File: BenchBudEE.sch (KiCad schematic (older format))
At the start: 0 parts

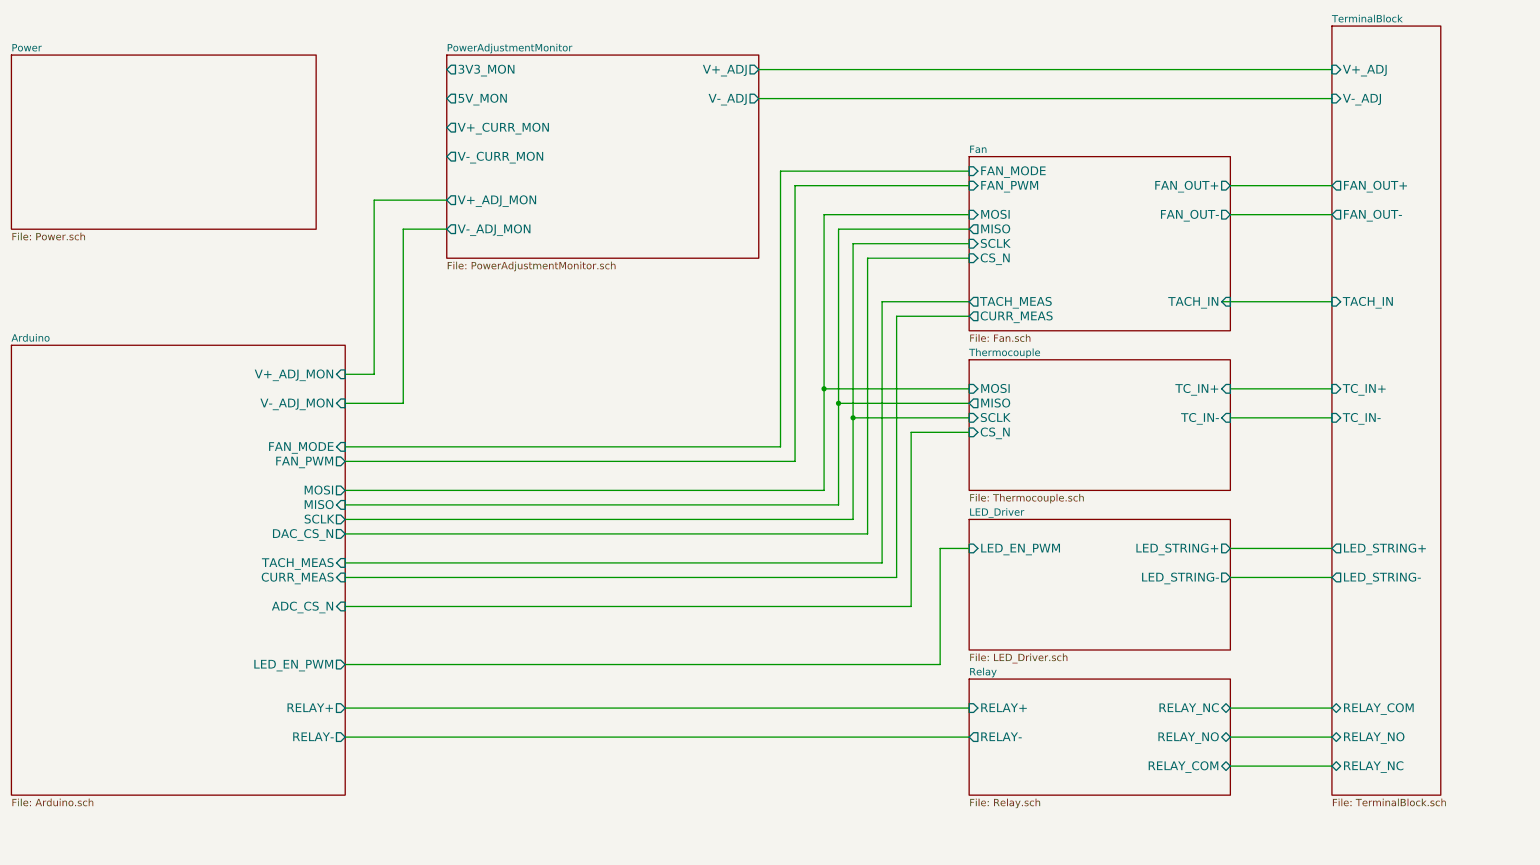
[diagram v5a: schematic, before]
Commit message: Associated and placed the thermocouple module
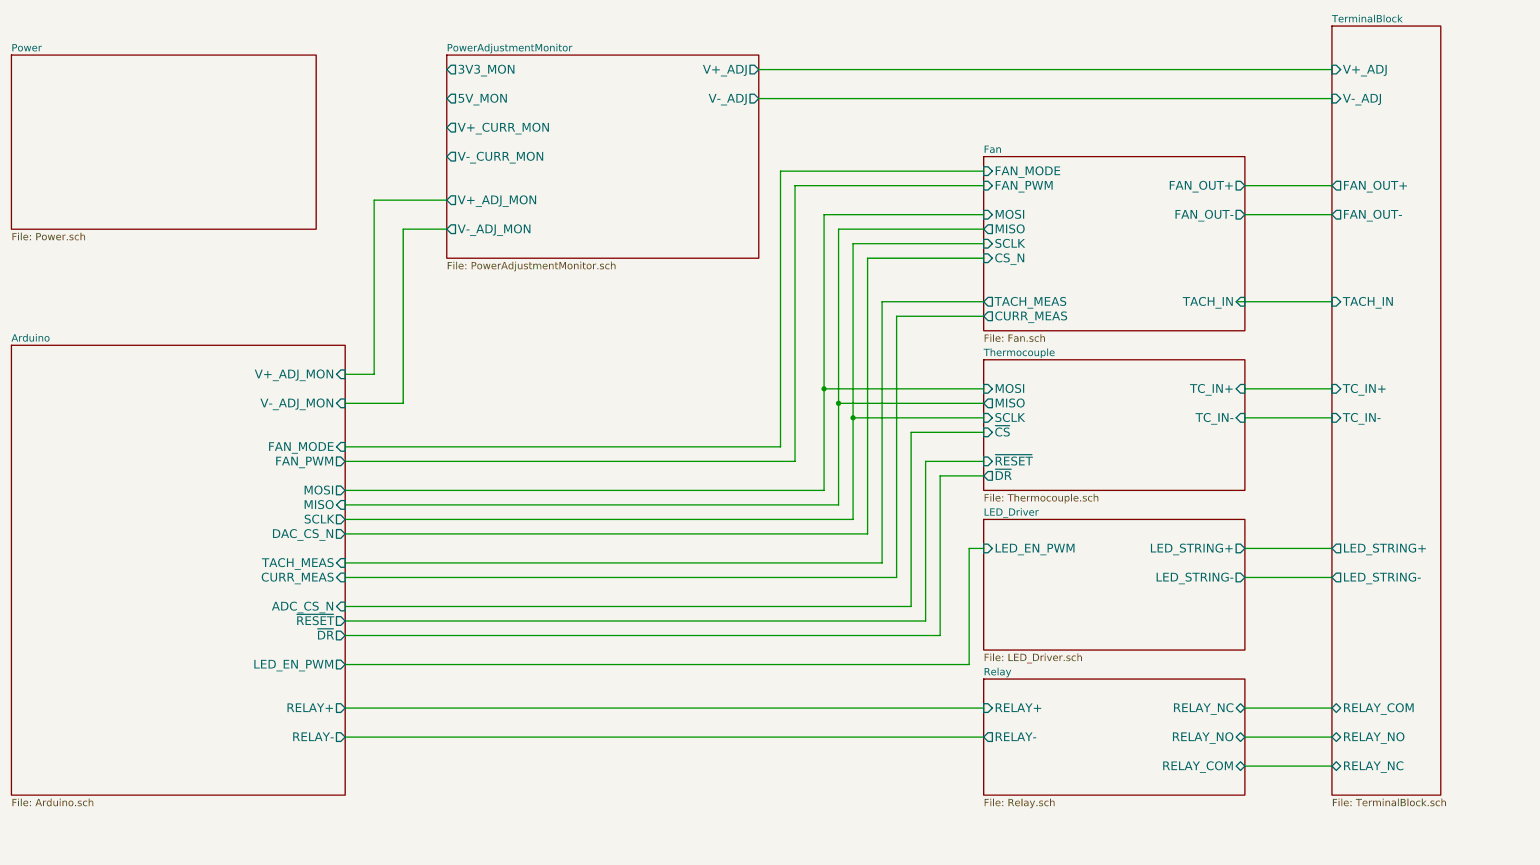
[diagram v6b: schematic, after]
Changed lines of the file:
@@
 $EndDescr
 $Sheet
-S 7500 5300 1800 800
+S 7600 5300 1800 800
 U 52EAE4BD
 F0 "Relay" 50
 F1 "Relay.sch" 50
-F2 "RELAY_NC" B R 9300 5500 60
-F3 "RELAY_NO" B R 9300 5700 60
-F4 "RELAY_COM" B R 9300 5900 60
-F5 "RELAY+" I L 7500 5500 60
-F6 "RELAY-" O L 7500 5700 60
-$EndSheet
-$Sheet
-S 7500 4200 1800 900
+F2 "RELAY_NC" B R 9400 5500 60
+F3 "RELAY_NO" B R 9400 5700 60
+F4 "RELAY_COM" B R 9400 5900 60
+F5 "RELAY+" I L 7600 5500 60
+F6 "RELAY-" O L 7600 5700 60
+$EndSheet
+$Sheet
+S 7600 4200 1800 900
 U 52EAE512
 F0 "LED_Driver" 50
 F1 "LED_Driver.sch" 50
-F2 "LED_EN_PWM" I L 7500 4400 60
-F3 "LED_STRING+" O R 9300 4400 60
-F4 "LED_STRING-" O R 9300 4600 60
+F2 "LED_EN_PWM" I L 7600 4400 60
+F3 "LED_STRING+" O R 9400 4400 60
+F4 "LED_STRING-" O R 9400 4600 60
 $EndSheet
 $Sheet
@@
 	10000 1300 6050 1300
 Wire Wire Line
-	10000 1900 9300 1900
-Wire Wire Line
-	10000 2100 9300 2100
-Wire Wire Line
-	9250 2700 10000 2700
-Wire Wire Line
-	10000 3300 9300 3300
-Wire Wire Line
-	10000 3500 9300 3500
-Wire Wire Line
-	10000 4400 9300 4400
-Wire Wire Line
-	10000 4600 9300 4600
-Wire Wire Line
-	10000 5500 9300 5500
-Wire Wire Line
-	10000 5700 9300 5700
-Wire Wire Line
-	10000 5900 9300 5900
+	10000 1900 9400 1900
+Wire Wire Line
+	10000 2100 9400 2100
+Wire Wire Line
+	9350 2700 10000 2700
+Wire Wire Line
+	10000 3300 9400 3300
+Wire Wire Line
+	10000 3500 9400 3500
+Wire Wire Line
+	10000 4400 9400 4400
+Wire Wire Line
+	10000 4600 9400 4600
+Wire Wire Line
+	10000 5500 9400 5500
+Wire Wire Line
+	10000 5700 9400 5700
+Wire Wire Line
+	10000 5900 9400 5900
 Wire Wire Line
 	3200 3200 3400 3200
@@
 	6300 3800 6300 1900
 Wire Wire Line
-	6300 1900 7500 1900
+	6300 1900 7600 1900
 Wire Wire Line
 	6500 4000 3200 4000
@@
 	6500 2100 6500 4000
 Wire Wire Line
-	6500 2100 7500 2100
+	6500 2100 7600 2100
 Wire Wire Line
 	6600 4100 3200 4100
@@
 	6600 2200 6600 4100
 Wire Wire Line
-	6600 2200 7500 2200
+	6600 2200 7600 2200
 Wire Wire Line
 	6700 4200 3200 4200
@@
 	6700 2300 6700 4200
 Wire Wire Line
-	6700 2300 7500 2300
+	6700 2300 7600 2300
 Wire Wire Line
 	3200 4300 6800 4300
@@
 	6800 4300 6800 2400
 Wire Wire Line
-	6800 2400 7500 2400
+	6800 2400 7600 2400
 Wire Wire Line
 	3200 4500 6900 4500
@@
 	6900 4500 6900 2700
 Wire Wire Line
-	6900 2700 7500 2700
+	6900 2700 7600 2700
 Wire Wire Line
 	3200 4600 7000 4600
@@
 	7000 4600 7000 2800
 Wire Wire Line
-	7000 2800 7500 2800
-$Sheet
-S 7500 1700 1800 1200
+	7000 2800 7600 2800
+$Sheet
+S 7600 1700 1800 1200
 U 52EAE52A
 F0 "Fan" 50
 F1 "Fan.sch" 50
-F2 "MOSI" I L 7500 2100 60
-F3 "MISO" O L 7500 2200 60
-F4 "CS_N" I L 7500 2400 60
-F5 "SCLK" I L 7500 2300 60
-F6 "FAN_OUT+" O R 9300 1900 60
-F7 "TACH_IN" I R 9300 2700 60
-F8 "TACH_MEAS" O L 7500 2700 60
-F9 "CURR_MEAS" O L 7500 2800 60
-F10 "FAN_OUT-" O R 9300 2100 60
-F11 "FAN_PWM" I L 7500 1900 60
-F12 "FAN_MODE" I L 7500 1800 60
-$EndSheet
-$Sheet
-S 7500 3100 1800 900
+F2 "MOSI" I L 7600 2100 60
+F3 "MISO" O L 7600 2200 60
+F4 "CS_N" I L 7600 2400 60
+F5 "SCLK" I L 7600 2300 60
+F6 "FAN_OUT+" O R 9400 1900 60
+F7 "TACH_IN" I R 9400 2700 60
+F8 "TACH_MEAS" O L 7600 2700 60
+F9 "CURR_MEAS" O L 7600 2800 60
+F10 "FAN_OUT-" O R 9400 2100 60
+F11 "FAN_PWM" I L 7600 1900 60
+F12 "FAN_MODE" I L 7600 1800 60
+$EndSheet
+$Sheet
+S 7600 3100 1800 900
 U 52EAE493
 F0 "Thermocouple" 50
 F1 "Thermocouple.sch" 50
-F2 "TC_IN+" I R 9300 3300 60
-F3 "TC_IN-" I R 9300 3500 60
-F4 "MOSI" I L 7500 3300 60
-F5 "MISO" O L 7500 3400 60
-F6 "SCLK" I L 7500 3500 60
-F7 "CS_N" I L 7500 3600 60
+F2 "TC_IN+" I R 9400 3300 60
+F3 "TC_IN-" I R 9400 3500 60
+F4 "MOSI" I L 7600 3300 60
+F5 "MISO" O L 7600 3400 60
+F6 "SCLK" I L 7600 3500 60
+F7 "~CS" I L 7600 3600 60
+F8 "~DR" O L 7600 3900 60
+F9 "~RESET" I L 7600 3800 60
 $EndSheet
 $Sheet
@@
 F14 "FAN_PWM" O R 3200 3800 60
 F15 "FAN_MODE" I R 3200 3700 60
+F16 "~RESET" O R 3200 4900 60
+F17 "~DR" O R 3200 5000 60
 $EndSheet
 Wire Wire Line
@@
 	7100 4800 7100 3600
 Wire Wire Line
-	7100 3600 7500 3600
-Wire Wire Line
-	7500 3500 6700 3500
+	7100 3600 7600 3600
+Wire Wire Line
+	7600 3500 6700 3500
 Connection ~ 6700 3500
 Wire Wire Line
-	7500 3400 6600 3400
+	7600 3400 6600 3400
 Connection ~ 6600 3400
 Wire Wire Line
-	7500 3300 6500 3300
+	7600 3300 6500 3300
 Connection ~ 6500 3300
 Wire Wire Line
-	3200 5200 7300 5200
-Wire Wire Line
-	7300 5200 7300 4400
-Wire Wire Line
-	7300 4400 7500 4400
-Wire Wire Line
-	3200 5500 7500 5500
-Wire Wire Line
-	7500 5700 3200 5700
-Wire Wire Line
-	7500 1800 6200 1800
+	3200 5200 7500 5200
+Wire Wire Line
+	7500 5200 7500 4400
+Wire Wire Line
+	7500 4400 7600 4400
+Wire Wire Line
+	3200 5500 7600 5500
+Wire Wire Line
+	7600 5700 3200 5700
+Wire Wire Line
+	7600 1800 6200 1800
 Wire Wire Line
 	6200 1800 6200 3700
 Wire Wire Line
 	6200 3700 3200 3700
+Wire Wire Line
+	7600 3800 7200 3800
+Wire Wire Line
+	7200 3800 7200 4900
+Wire Wire Line
+	7200 4900 3200 4900
+Wire Wire Line
+	7600 3900 7300 3900
+Wire Wire Line
+	7300 3900 7300 5000
+Wire Wire Line
+	7300 5000 3200 5000
 $EndSCHEMATC

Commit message: Associated and placed the Current/Fan Driver Module
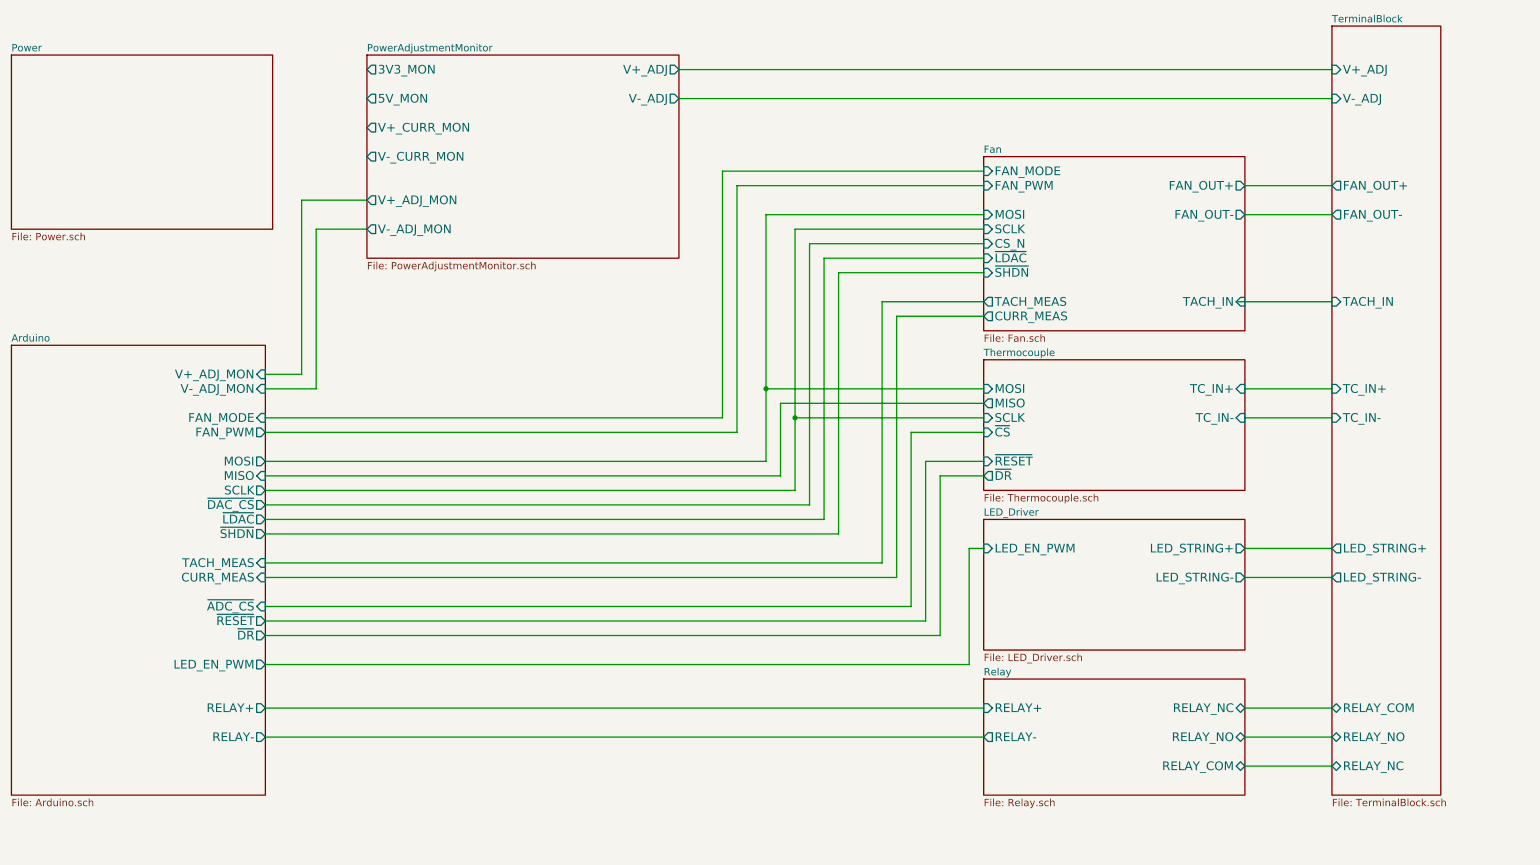
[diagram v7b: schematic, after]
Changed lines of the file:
@@
 $EndSheet
 $Sheet
-S 900  1000 2100 1200
+S 900  1000 1800 1200
 U 52EAE4E0
 F0 "Power" 50
@@
 $EndSheet
 $Sheet
-S 3900 1000 2150 1400
+S 3350 1000 2150 1400
 U 52F17012
 F0 "PowerAdjustmentMonitor" 50
 F1 "PowerAdjustmentMonitor.sch" 50
-F2 "V+_ADJ" O R 6050 1100 60
-F3 "V-_ADJ" O R 6050 1300 60
-F4 "3V3_MON" O L 3900 1100 60
-F5 "5V_MON" O L 3900 1300 60
-F6 "V+_ADJ_MON" O L 3900 2000 60
-F7 "V-_ADJ_MON" O L 3900 2200 60
-F8 "V+_CURR_MON" O L 3900 1500 60
-F9 "V-_CURR_MON" O L 3900 1700 60
-$EndSheet
-Wire Wire Line
-	10000 1100 6050 1100
-Wire Wire Line
-	10000 1300 6050 1300
-Wire Wire Line
-	10000 1900 9400 1900
-Wire Wire Line
-	10000 2100 9400 2100
-Wire Wire Line
-	9350 2700 10000 2700
-Wire Wire Line
-	10000 3300 9400 3300
-Wire Wire Line
-	10000 3500 9400 3500
-Wire Wire Line
-	10000 4400 9400 4400
-Wire Wire Line
-	10000 4600 9400 4600
-Wire Wire Line
-	10000 5500 9400 5500
-Wire Wire Line
-	10000 5700 9400 5700
-Wire Wire Line
-	10000 5900 9400 5900
-Wire Wire Line
-	3200 3200 3400 3200
-Wire Wire Line
-	3400 3200 3400 2000
-Wire Wire Line
-	3400 2000 3900 2000
-Wire Wire Line
-	3200 3400 3600 3400
-Wire Wire Line
-	3600 3400 3600 2200
-Wire Wire Line
-	3600 2200 3900 2200
-Wire Wire Line
-	3200 3800 6300 3800
-Wire Wire Line
-	6300 3800 6300 1900
-Wire Wire Line
-	6300 1900 7600 1900
-Wire Wire Line
-	6500 4000 3200 4000
-Wire Wire Line
-	6500 2100 6500 4000
-Wire Wire Line
-	6500 2100 7600 2100
-Wire Wire Line
-	6600 4100 3200 4100
-Wire Wire Line
-	6600 2200 6600 4100
-Wire Wire Line
-	6600 2200 7600 2200
-Wire Wire Line
-	6700 4200 3200 4200
-Wire Wire Line
-	6700 2300 6700 4200
-Wire Wire Line
-	6700 2300 7600 2300
-Wire Wire Line
-	3200 4300 6800 4300
-Wire Wire Line
-	6800 4300 6800 2400
-Wire Wire Line
-	6800 2400 7600 2400
-Wire Wire Line
-	3200 4500 6900 4500
-Wire Wire Line
-	6900 4500 6900 2700
-Wire Wire Line
-	6900 2700 7600 2700
-Wire Wire Line
-	3200 4600 7000 4600
-Wire Wire Line
-	7000 4600 7000 2800
-Wire Wire Line
-	7000 2800 7600 2800
+F2 "V+_ADJ" O R 5500 1100 60
+F3 "V-_ADJ" O R 5500 1300 60
+F4 "3V3_MON" O L 3350 1100 60
+F5 "5V_MON" O L 3350 1300 60
+F6 "V+_ADJ_MON" O L 3350 2000 60
+F7 "V-_ADJ_MON" O L 3350 2200 60
+F8 "V+_CURR_MON" O L 3350 1500 60
+F9 "V-_CURR_MON" O L 3350 1700 60
+$EndSheet
 $Sheet
 S 7600 1700 1800 1200
@@
 F1 "Fan.sch" 50
 F2 "MOSI" I L 7600 2100 60
-F3 "MISO" O L 7600 2200 60
-F4 "CS_N" I L 7600 2400 60
-F5 "SCLK" I L 7600 2300 60
-F6 "FAN_OUT+" O R 9400 1900 60
-F7 "TACH_IN" I R 9400 2700 60
-F8 "TACH_MEAS" O L 7600 2700 60
-F9 "CURR_MEAS" O L 7600 2800 60
-F10 "FAN_OUT-" O R 9400 2100 60
-F11 "FAN_PWM" I L 7600 1900 60
-F12 "FAN_MODE" I L 7600 1800 60
+F3 "CS_N" I L 7600 2300 60
+F4 "SCLK" I L 7600 2200 60
+F5 "FAN_OUT+" O R 9400 1900 60
+F6 "TACH_IN" I R 9400 2700 60
+F7 "TACH_MEAS" O L 7600 2700 60
+F8 "CURR_MEAS" O L 7600 2800 60
+F9 "FAN_OUT-" O R 9400 2100 60
+F10 "FAN_PWM" I L 7600 1900 60
+F11 "FAN_MODE" I L 7600 1800 60
+F12 "~LDAC" I L 7600 2400 60
+F13 "~SHDN" I L 7600 2500 60
 $EndSheet
 $Sheet
@@
 $EndSheet
 $Sheet
-S 900  3000 2300 3100
+S 900  3000 1750 3100
 U 52EAE42B
 F0 "Arduino" 50
 F1 "Arduino.sch" 50
-F2 "MOSI" O R 3200 4000 60
-F3 "MISO" I R 3200 4100 60
-F4 "TACH_MEAS" I R 3200 4500 60
-F5 "SCLK" O R 3200 4200 60
-F6 "CURR_MEAS" I R 3200 4600 60
-F7 "RELAY+" O R 3200 5500 60
-F8 "RELAY-" O R 3200 5700 60
-F9 "V+_ADJ_MON" I R 3200 3200 60
-F10 "V-_ADJ_MON" I R 3200 3400 60
-F11 "LED_EN_PWM" O R 3200 5200 60
-F12 "DAC_CS_N" O R 3200 4300 60
-F13 "ADC_CS_N" I R 3200 4800 60
-F14 "FAN_PWM" O R 3200 3800 60
-F15 "FAN_MODE" I R 3200 3700 60
-F16 "~RESET" O R 3200 4900 60
-F17 "~DR" O R 3200 5000 60
-$EndSheet
-Wire Wire Line
-	3200 4800 7100 4800
+F2 "MOSI" O R 2650 3800 60
+F3 "MISO" I R 2650 3900 60
+F4 "TACH_MEAS" I R 2650 4500 60
+F5 "SCLK" O R 2650 4000 60
+F6 "CURR_MEAS" I R 2650 4600 60
+F7 "RELAY+" O R 2650 5500 60
+F8 "RELAY-" O R 2650 5700 60
+F9 "V+_ADJ_MON" I R 2650 3200 60
+F10 "V-_ADJ_MON" I R 2650 3300 60
+F11 "LED_EN_PWM" O R 2650 5200 60
+F12 "FAN_PWM" O R 2650 3600 60
+F13 "FAN_MODE" I R 2650 3500 60
+F14 "~RESET" O R 2650 4900 60
+F15 "~DR" O R 2650 5000 60
+F16 "~LDAC" O R 2650 4200 60
+F17 "~SHDN" O R 2650 4300 60
+F18 "~DAC_CS" O R 2650 4100 60
+F19 "~ADC_CS" I R 2650 4800 60
+$EndSheet
+Wire Wire Line
+	6200 3900 6200 3400
+Wire Wire Line
+	2650 5000 7300 5000
+Wire Wire Line
+	7300 5000 7300 3900
+Wire Wire Line
+	7300 3900 7600 3900
+Wire Wire Line
+	2650 4900 7200 4900
+Wire Wire Line
+	7200 4900 7200 3800
+Wire Wire Line
+	7200 3800 7600 3800
+Wire Wire Line
+	2650 3500 5800 3500
+Wire Wire Line
+	5800 3500 5800 1800
+Wire Wire Line
+	5800 1800 7600 1800
+Wire Wire Line
+	2650 5700 7600 5700
+Wire Wire Line
+	2650 5500 7600 5500
+Wire Wire Line
+	7500 4400 7600 4400
+Wire Wire Line
+	7500 5200 7500 4400
+Wire Wire Line
+	2650 5200 7500 5200
+Connection ~ 6100 3300
+Wire Wire Line
+	7600 3300 6100 3300
+Wire Wire Line
+	6200 3400 7600 3400
+Connection ~ 6300 3500
+Wire Wire Line
+	7600 3500 6300 3500
+Wire Wire Line
+	7100 3600 7600 3600
 Wire Wire Line
 	7100 4800 7100 3600
 Wire Wire Line
-	7100 3600 7600 3600
-Wire Wire Line
-	7600 3500 6700 3500
-Connection ~ 6700 3500
-Wire Wire Line
-	7600 3400 6600 3400
-Connection ~ 6600 3400
-Wire Wire Line
-	7600 3300 6500 3300
-Connection ~ 6500 3300
-Wire Wire Line
-	3200 5200 7500 5200
-Wire Wire Line
-	7500 5200 7500 4400
-Wire Wire Line
-	7500 4400 7600 4400
-Wire Wire Line
-	3200 5500 7600 5500
-Wire Wire Line
-	7600 5700 3200 5700
-Wire Wire Line
-	7600 1800 6200 1800
-Wire Wire Line
-	6200 1800 6200 3700
-Wire Wire Line
-	6200 3700 3200 3700
-Wire Wire Line
-	7600 3800 7200 3800
-Wire Wire Line
-	7200 3800 7200 4900
-Wire Wire Line
-	7200 4900 3200 4900
-Wire Wire Line
-	7600 3900 7300 3900
-Wire Wire Line
-	7300 3900 7300 5000
-Wire Wire Line
-	7300 5000 3200 5000
+	2650 4800 7100 4800
+Wire Wire Line
+	7000 2800 7600 2800
+Wire Wire Line
+	7000 4600 7000 2800
+Wire Wire Line
+	2650 4600 7000 4600
+Wire Wire Line
+	6900 2700 7600 2700
+Wire Wire Line
+	6900 4500 6900 2700
+Wire Wire Line
+	2650 4500 6900 4500
+Wire Wire Line
+	6400 2300 7600 2300
+Wire Wire Line
+	6400 4100 6400 2300
+Wire Wire Line
+	2650 4100 6400 4100
+Wire Wire Line
+	6300 2200 7600 2200
+Wire Wire Line
+	6300 2200 6300 4000
+Wire Wire Line
+	6300 4000 2650 4000
+Wire Wire Line
+	2650 3900 6200 3900
+Wire Wire Line
+	6100 2100 7600 2100
+Wire Wire Line
+	6100 2100 6100 3800
+Wire Wire Line
+	6100 3800 2650 3800
+Wire Wire Line
+	5900 1900 7600 1900
+Wire Wire Line
+	5900 3600 5900 1900
+Wire Wire Line
+	2650 3600 5900 3600
+Wire Wire Line
+	3000 2200 3350 2200
+Wire Wire Line
+	3000 3300 3000 2200
+Wire Wire Line
+	2650 3300 3000 3300
+Wire Wire Line
+	2900 2000 3350 2000
+Wire Wire Line
+	2900 3200 2900 2000
+Wire Wire Line
+	2650 3200 2900 3200
+Wire Wire Line
+	10000 5900 9400 5900
+Wire Wire Line
+	10000 5700 9400 5700
+Wire Wire Line
+	10000 5500 9400 5500
+Wire Wire Line
+	10000 4600 9400 4600
+Wire Wire Line
+	10000 4400 9400 4400
+Wire Wire Line
+	10000 3500 9400 3500
+Wire Wire Line
+	10000 3300 9400 3300
+Wire Wire Line
+	9350 2700 10000 2700
+Wire Wire Line
+	10000 2100 9400 2100
+Wire Wire Line
+	10000 1900 9400 1900
+Wire Wire Line
+	10000 1300 5500 1300
+Wire Wire Line
+	10000 1100 5500 1100
+Wire Wire Line
+	2650 4200 6500 4200
+Wire Wire Line
+	6500 4200 6500 2400
+Wire Wire Line
+	6500 2400 7600 2400
+Wire Wire Line
+	2650 4300 6600 4300
+Wire Wire Line
+	6600 4300 6600 2500
+Wire Wire Line
+	6600 2500 7600 2500
 $EndSCHEMATC

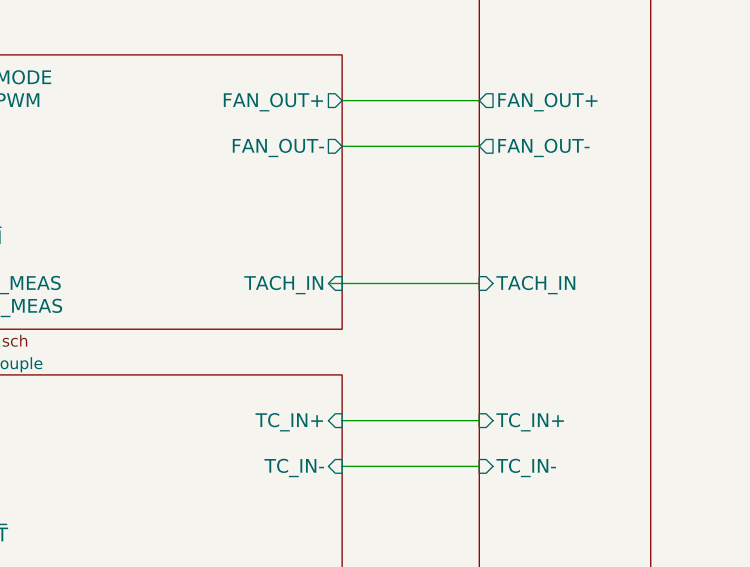
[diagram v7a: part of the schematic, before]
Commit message: Rearranged layout a bit and added heatsinks
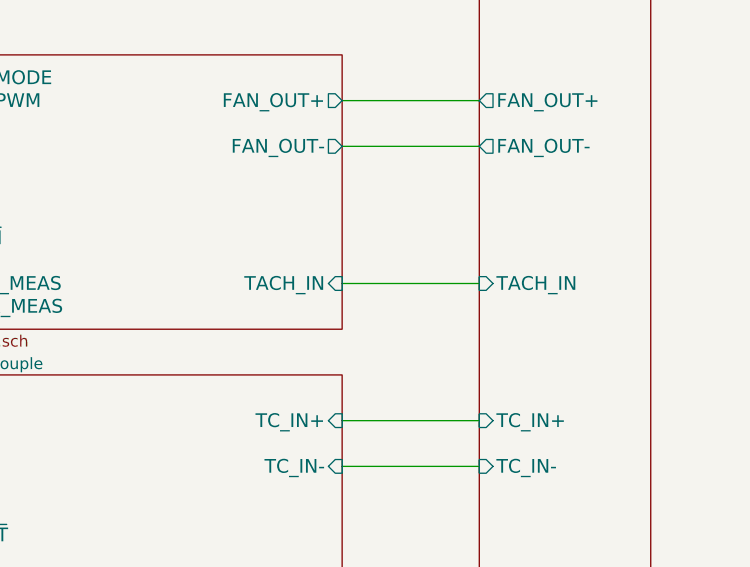
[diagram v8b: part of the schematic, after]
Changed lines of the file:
@@
 	10000 3300 9400 3300
-Wire Wire Line
-	9350 2700 10000 2700
 Wire Wire Line
 	10000 2100 9400 2100
@@
 Wire Wire Line
 	6600 2500 7600 2500
+Wire Wire Line
+	10000 2700 9400 2700
 $EndSCHEMATC
